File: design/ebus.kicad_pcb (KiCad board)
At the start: 2 copper layers, 84.3 x 56.9 mm, 49 parts, among them J1 EBUS

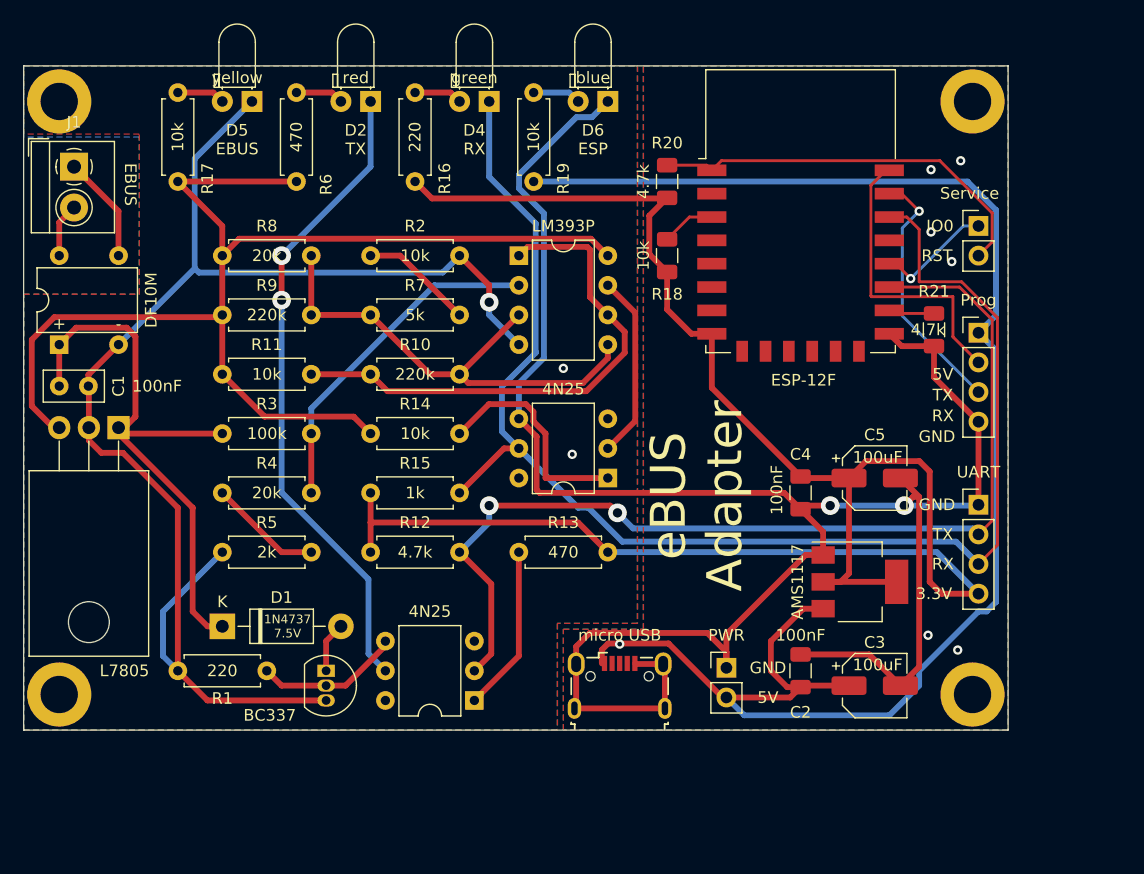
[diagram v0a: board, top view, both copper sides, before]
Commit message: Voltage regulator changes, some graphical improvements of pcb
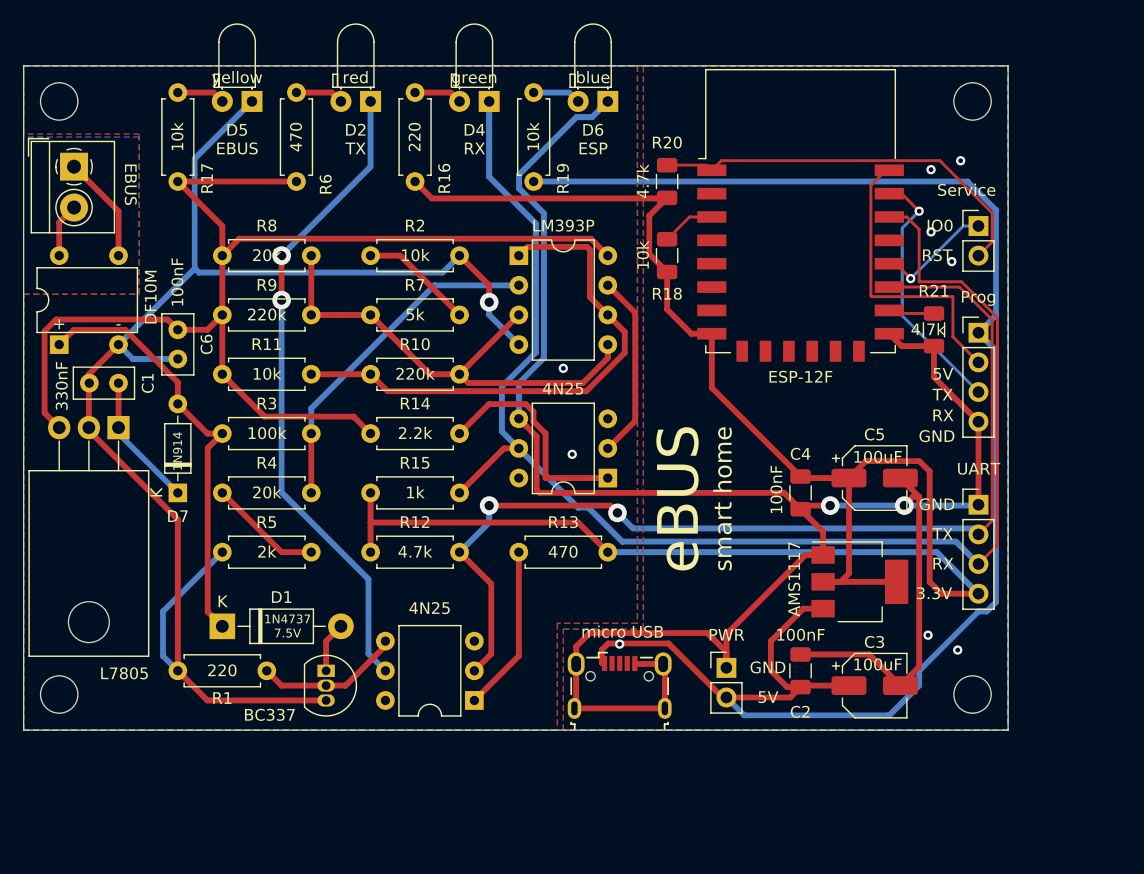
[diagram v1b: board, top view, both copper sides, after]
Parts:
- removed the REF** at (121.4, 136.7)
- removed the REF** at (121.4, 85.9)
- removed the REF** at (43.2, 85.9)
- removed the REF** at (43.2, 136.7)
- added C6: 100nF, Capacitor_THT:C_Disc_D5.0mm_W2.5mm_P2.50mm, F.Cu at (53.3, 105.4)
- added D7: 1N914, Diode_THT:D_DO-35_SOD27_P7.62mm_Horizontal, F.Cu at (53.3, 119.4)
- added REF**: MountingHole_3.2mm_M3_ISO14580, MountingHole:MountingHole_3.2mm_M3_ISO14580, F.Cu at (121.4, 136.7)
- added REF**: MountingHole_3.2mm_M3_ISO14580, MountingHole:MountingHole_3.2mm_M3_ISO14580, F.Cu at (121.4, 85.9)
- added REF**: MountingHole_3.2mm_M3_ISO14580, MountingHole:MountingHole_3.2mm_M3_ISO14580, F.Cu at (43.2, 136.7)
- added REF**: MountingHole_3.2mm_M3_ISO14580, MountingHole:MountingHole_3.2mm_M3_ISO14580, F.Cu at (43.2, 85.9)
- C1: value 100nF -> 330nF
- J3: renamed from micro USB
- R14: value 10k -> 2.2k
- moved C1 5.09 mm to (48.3, 110.0), turned to 180 degrees
- renumbered DF10M to D3, UART to J2, PWR to J4, Service to J5, Prog to J6, BC337 to Q1, LM393P to U1, 4N25 to U2, L7805 to U3, 4N25 to U4, ESP-12F to U5, AMS1117 to U6
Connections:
- C1 pad 1: SIGNAL -> Net-(C1-Pad1)
- U3 pad 1: SIGNAL -> Net-(C1-Pad1)
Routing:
- net SIGNAL: track 49.7 -> 36.8 mm
- net Net-(C1-Pad1): track 0.00 -> 11.5 mm
- net GNDD: track 118.0 -> 123.0 mm
- net +5V: track 103.9 -> 102.6 mm
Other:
- board text added: "1N914"
- board text added: "2.2k"
- board text added: "330nF"
- board text added: "4N25"
- board text added: "AMS1117"
- board text added: "BC337"
- board text added: "DF10M"
- board text added: "ESP-12F"
- board text added: "L7805"
- board text added: "LM393P"
- board text added: "PWR"
- board text added: "Prog"
- board text added: "Service"
- board text added: "UART"
- board text added: "eBUS"
- board text added: "micro USB"
- board text added: "smart home"
- board text removed: "eBUS Adapter"

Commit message: SMD PCB for Raspberry PI Zero
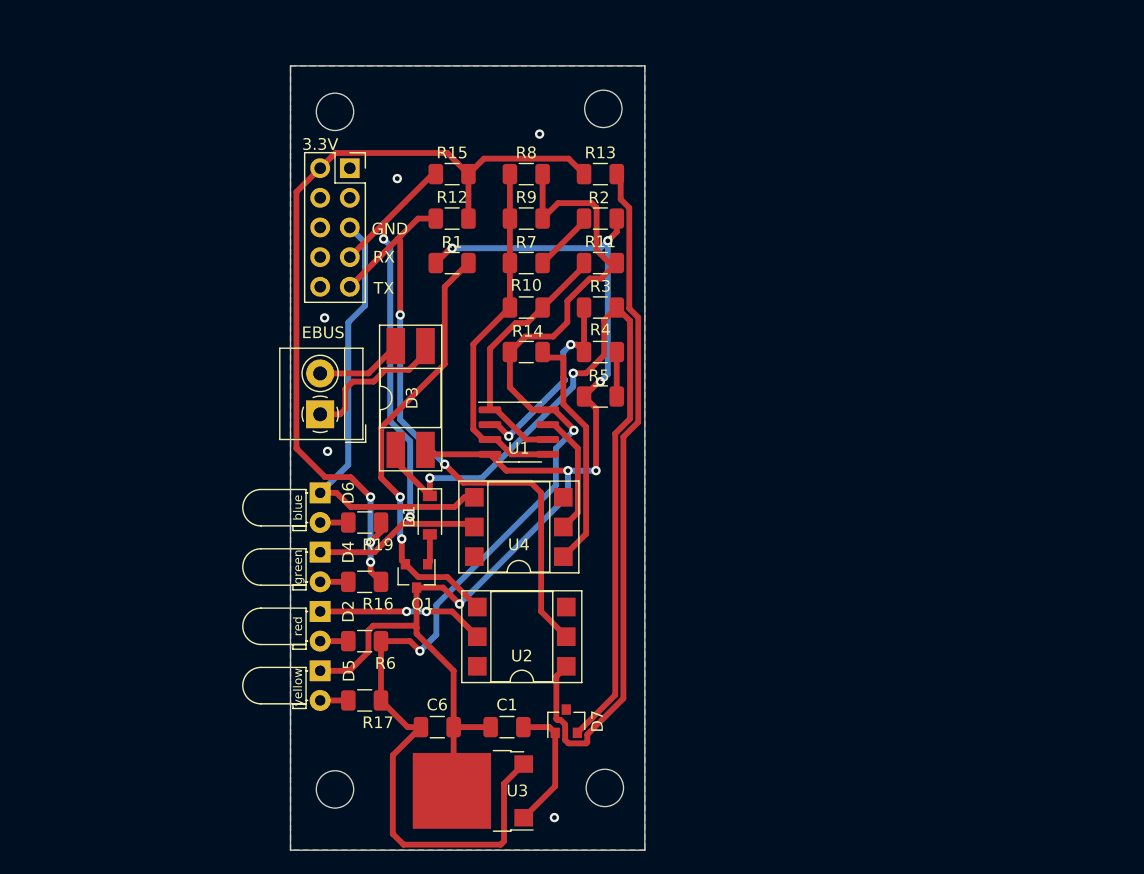
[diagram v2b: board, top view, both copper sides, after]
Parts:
- removed C2, C4: 100nF, Capacitor_SMD:C_1206_3216Metric
- removed C3, C5: 100uF, Capacitor_SMD:CP_Elec_5x5.7
- removed J2: UART, Connector_PinHeader_2.54mm:PinHeader_1x04_P2.54mm_Vertical
- removed J4: PWR, Connector_PinHeader_2.54mm:PinHeader_1x02_P2.54mm_Vertical
- removed J5: SERVICE, Connector_PinHeader_2.54mm:PinHeader_1x02_P2.54mm_Vertical
- removed J6: PROG, Connector_PinHeader_2.54mm:PinHeader_1x04_P2.54mm_Vertical
- removed R18: 10k, Resistor_SMD:R_1206_3216Metric
- removed R20, R21: 4.7k, Resistor_SMD:R_1206_3216Metric
- removed REF** (x4): MountingHole_3.2mm_M3_ISO14580, MountingHole:MountingHole_3.2mm_M3_ISO14580
- removed U5: ESP-12F, RF_Module:ESP-12E
- removed U6: AMS1117-3.3, Package_TO_SOT_SMD:SOT-223-3_TabPin2
- added H1: MountingHole, MountingHole:MountingHole_3.2mm_M3, F.Cu at (66.8, 86.7)
- added H2: MountingHole, MountingHole:MountingHole_3.2mm_M3, F.Cu at (66.8, 144.8)
- added H3: MountingHole, MountingHole:MountingHole_3.2mm_M3, F.Cu at (89.8, 86.5)
- added H4: MountingHole, MountingHole:MountingHole_3.2mm_M3, F.Cu at (89.9, 144.7)
- C1, C6: footprint Capacitor_THT:C_Disc_D5.0mm_W2.5mm_P2.50mm -> Capacitor_SMD:C_1206_3216Metric
- D1: footprint Diode_THT:D_DO-41_SOD81_P10.16mm_Horizontal -> Diode_SMD:D_SOD-123
- D3: footprint Diode_THT:Diode_Bridge_DIP-4_W7.62mm_P5.08mm -> Package_DIP:DIP-4_W8.89mm_SMDSocket_LongPads
- D7: footprint Diode_THT:D_DO-35_SOD27_P7.62mm_Horizontal -> Package_TO_SOT_SMD:SOT-23
- J3: value USB_B_Micro -> UART; footprint Connector_USB:USB_Micro-B_Wuerth_629105150521 -> Connector_PinSocket_2.54mm:PinSocket_2x05_P2.54mm_Vertical
- Q1: footprint Package_TO_SOT_THT:TO-92_Inline -> Package_TO_SOT_SMD:SOT-23
- R1, R10, R11, R12, R13, R14, R15, R16, R17, R19, R2, R3, R4, R5, R6, R7, R8, R9: footprint Resistor_THT:R_Axial_DIN0207_L6.3mm_D2.5mm_P7.62mm_Horizontal -> Resistor_SMD:R_1206_3216Metric
- U1: footprint Package_DIP:DIP-8_W7.62mm -> Package_SO:SOIC-8_3.9x4.9mm_P1.27mm
- U2, U4: footprint Package_DIP:DIP-6_W7.62mm -> Package_DIP:DIP-6_W7.62mm_SMDSocket_SmallPads
- U3: footprint Package_TO_SOT_THT:TO-220-3_Horizontal_TabDown -> Package_TO_SOT_SMD:ATPAK-2
- moved R17 54.5 mm to (69.3, 137.2), turned to 0 degrees
- moved J3 50.0 mm to (68.1, 91.6)
- moved D5 49.1 mm to (65.5, 134.6), turned to 270 degrees
- moved R6 47.4 mm to (69.3, 132.1), turned to 0 degrees
- moved C1 44.4 mm to (81.5, 139.4)
- moved D2 43.9 mm to (65.5, 129.5), turned to 270 degrees
- moved U3 43.5 mm to (78.6, 144.9)
- moved R16 42.1 mm to (69.3, 127.0), turned to 0 degrees
- moved D6 41.6 mm to (65.5, 119.4), turned to 270 degrees
- moved D4 41.2 mm to (65.5, 124.5), turned to 270 degrees
- moved C6 40.6 mm to (75.6, 139.4), turned to 0 degrees
- moved R19 39.6 mm to (69.3, 121.9), turned to 0 degrees
- moved D7 38.6 mm to (86.6, 138.9)
- moved R1 38.4 mm to (76.8, 99.7)
- moved R5 35.0 mm to (89.5, 111.1)
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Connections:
- J3 pad 1: +5VP -> (no net)
- J3 pad 2: (no net) -> +3V3
- J3 pad 6: GNDREF -> (no net)
- R19 pad 2: +5VP -> +3V3
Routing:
- net GNDREF: track 182.2 -> 38.9 mm, vias 8 -> 0
- net +5VP: track 140.1 -> 0.00 mm, vias 1 -> 0
- net +3V3: track 155.9 -> 71.4 mm, vias 0 -> 3
- net RX: track 120.6 -> 51.3 mm, vias 0 -> 2
- net Net-(R13-Pad2): track 14.3 -> 60.4 mm
- net Net-(D2-Pad1): track 55.6 -> 14.4 mm
- net TX: track 88.7 -> 53.3 mm
- net RESET: track 34.4 -> 0.00 mm
- net SIGNAL: track 36.8 -> 69.9 mm, vias 0 -> 2
- net P_TX: track 25.2 -> 0.00 mm
- net Net-(Q1-Pad2): track 12.5 -> 37.4 mm, vias 0 -> 2
- net Net-(R10-Pad1): track 45.4 -> 22.5 mm
- net P_RX: track 22.0 -> 0.00 mm, vias 1 -> 0
- net GNDD: track 123.0 -> 106.6 mm, vias 3 -> 11
- net Net-(R10-Pad2): track 42.1 -> 30.4 mm
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- removed copper zone on B.Cu, net GNDREF
- removed copper zone on F.Cu, net GNDREF
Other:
- board size 84.3 x 56.9 mm -> 30.4 x 67.2 mm
- board text removed: "+"
- board text removed: "-"
- board text removed: "100k"
- board text removed: "100nF"
- board text removed: "100uF"
- board text removed: "10k"
- board text removed: "1N4737 7.5V"
- board text removed: "1N914"
- board text removed: "1k"
- board text removed: "2.2k"
- board text removed: "20k"
- board text removed: "220"
- board text removed: "220k"
- board text removed: "2k"
- board text removed: "330nF"
- board text removed: "4.7k"
- board text removed: "470"
- board text removed: "4N25"
- board text removed: "5V"
- board text removed: "5k"
- board text removed: "AMS1117"
- board text removed: "BC337"
- board text removed: "DF10M"
- board text removed: "ESP"
- board text removed: "ESP-12F"
- board text removed: "IO0"
- board text removed: "L7805"
- board text removed: "LM393P"
- board text removed: "PWR"
- board text removed: "Prog"
- board text removed: "RST"
- board text removed: "Service"
- board text removed: "UART"
- board text removed: "micro USB"

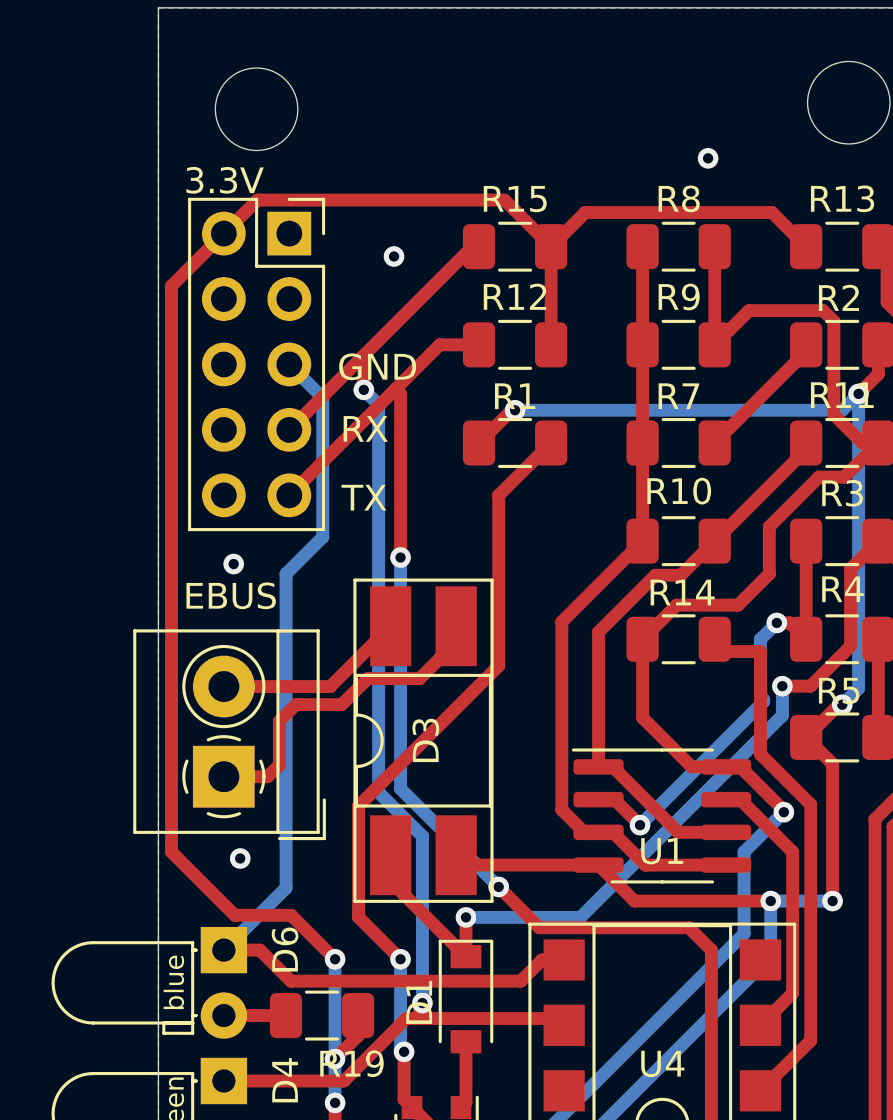
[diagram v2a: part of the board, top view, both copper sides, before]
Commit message: Fix for pins in wrong place
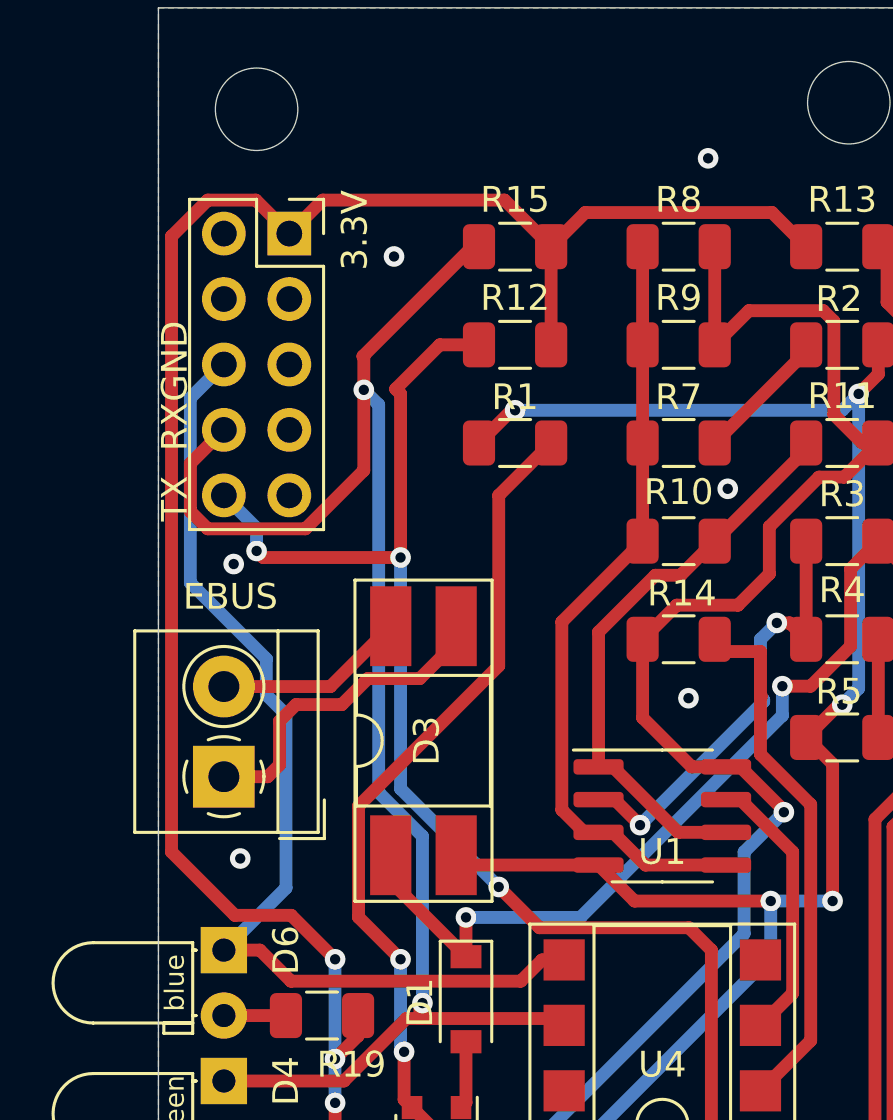
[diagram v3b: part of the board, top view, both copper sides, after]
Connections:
- J3 pad 1: (no net) -> +3V3
- J3 pad 10: (no net) -> TX
- J3 pad 2: +3V3 -> (no net)
- J3 pad 5: GNDREF -> (no net)
- J3 pad 6: (no net) -> GNDREF
- J3 pad 7: RX -> (no net)
- J3 pad 8: (no net) -> RX
- J3 pad 9: TX -> (no net)
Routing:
- net RX: track 51.3 -> 62.1 mm
- net TX: track 53.3 -> 55.8 mm, vias 2 -> 3
- net +3V3: track 71.4 -> 73.6 mm
- net GNDREF: track 38.9 -> 39.9 mm
- net GNDD: vias 11 -> 13

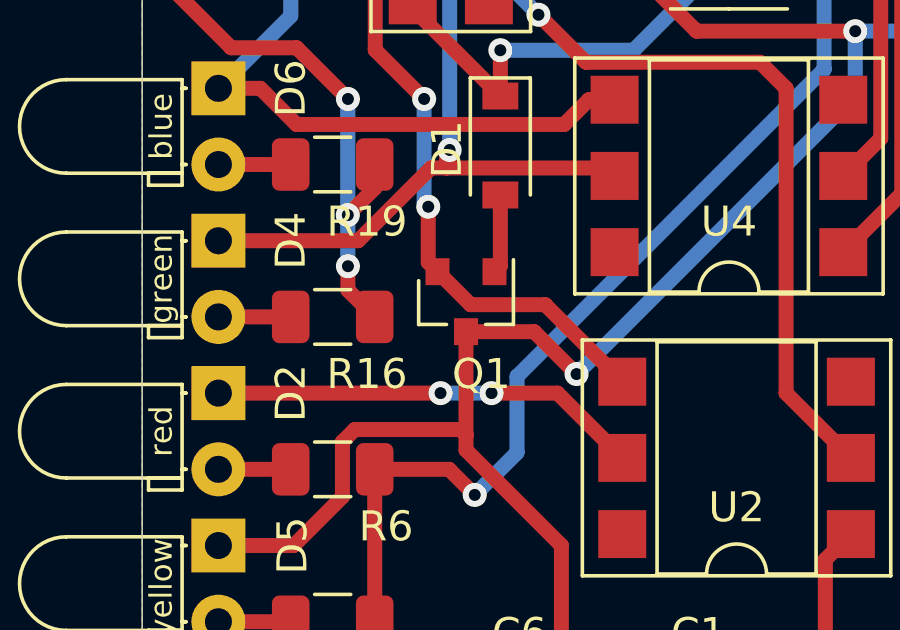
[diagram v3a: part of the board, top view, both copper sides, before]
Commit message: Wrong transistor case
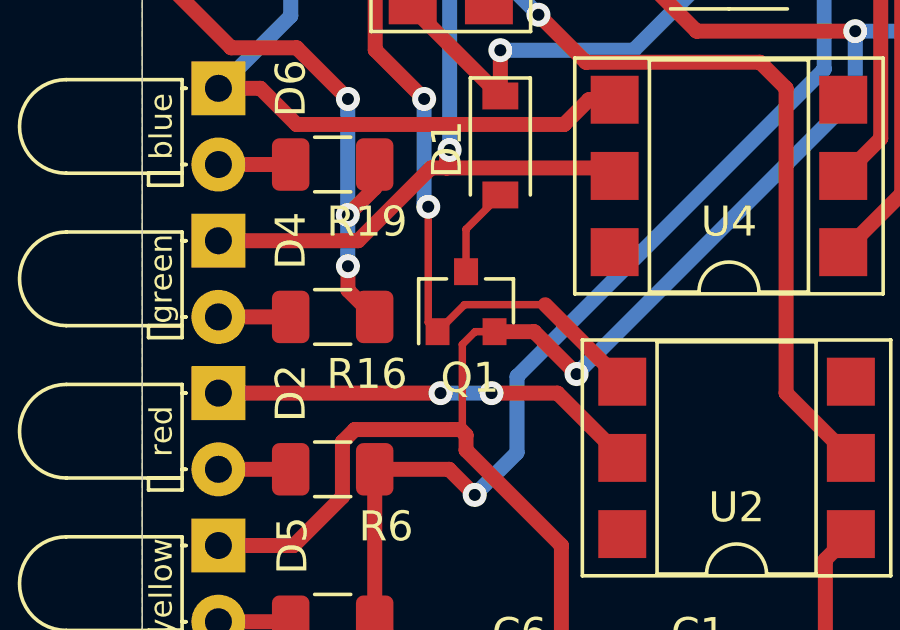
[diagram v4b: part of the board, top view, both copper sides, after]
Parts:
- Q1: value BC337 -> BC817
- turned Q1 to 90 degrees
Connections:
- Q1 pad 1: Net-(D1-Pad2) -> Net-(Q1-Pad1)
- Q1 pad 2: Net-(Q1-Pad2) -> GNDD
- Q1 pad 3: GNDD -> Net-(D1-Pad2)
- R1 pad 1: Net-(Q1-Pad2) -> Net-(Q1-Pad1)
- U2 pad 4: Net-(Q1-Pad2) -> Net-(Q1-Pad1)
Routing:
- net Net-(Q1-Pad1): track 0.00 -> 39.3 mm, vias 0 -> 2
- net Net-(Q1-Pad2): track 37.4 -> 0.00 mm, vias 2 -> 0

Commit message: Raspberry something
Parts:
- added C2: 100nF, Capacitor_SMD:C_1206_3216Metric, F.Cu at (114.0, 118.6)
- added C3: 100uF, Capacitor_SMD:CP_Elec_6.3x5.4, B.Cu at (113.6, 87.9)
- added C4: 100nF, Capacitor_SMD:C_1206_3216Metric, F.Cu at (113.9, 115.7)
- added C5: 100uF, Capacitor_SMD:CP_Elec_6.3x5.4, B.Cu at (106.3, 87.9)
- added J2: USB_B_Micro, Connector_USB:USB_Micro-B_Wuerth_629105150521, F.Cu at (121.4, 95.1)
- added J4: PROG, Connector_PinHeader_2.54mm:PinHeader_1x06_P2.54mm_Vertical, F.Cu at (132.4, 114.2)
- added J5: PINS, Connector_PinHeader_2.54mm:PinHeader_1x06_P2.54mm_Vertical, F.Cu at (132.7, 133.0)
- added J6: PWR, Connector_PinHeader_2.54mm:PinHeader_1x02_P2.54mm_Vertical, F.Cu at (132.3, 106.3)
- added J7: UART, Connector_PinHeader_2.54mm:PinHeader_2x05_P2.54mm_Vertical, F.Cu at (97.5, 91.6)
- added J8: switches, Connector_PinHeader_2.54mm:PinHeader_2x03_P2.54mm_Vertical, F.Cu at (107.3, 99.5)
- added R18: 10k, Resistor_SMD:R_1206_3216Metric, F.Cu at (102.2, 120.1)
- added R20: 4.7k, Resistor_SMD:R_1206_3216Metric, F.Cu at (107.8, 120.4)
- added U5: AMS1117-3.3, Package_TO_SOT_SMD:SOT-223-3_TabPin2, F.Cu at (107.5, 87.1)
- added U6: ESP-12F, RF_Module:ESP-12E, F.Cu at (110.0, 137.6)
- R1: value 220 -> 4.7k
- R12: value 4.7k -> X 4.7k
- R15: value 1k -> X 1k
- R19: value 10k -> 100k
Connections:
- net Net-(D3-Pad4) renamed +24V
- J3 pad 10: TX -> RX
- J3 pad 8: RX -> TX
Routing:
- net TX: track 55.8 -> 60.3 mm, vias 3 -> 2
- net RX: track 62.1 -> 59.6 mm
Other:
- board size 30.4 x 67.2 mm -> 61.7 x 67.2 mm
